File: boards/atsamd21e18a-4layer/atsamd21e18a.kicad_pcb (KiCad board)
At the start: 4 copper layers, 17.8 x 38.1 mm, 25 parts, among them J1 USB_B_Micro, J2 A, J3 B, J4 SWD_1.27, SW1 RESET, U1 AP7361C_SOT-89-5, U2 ATSAMD21E, Y1 <32MHz

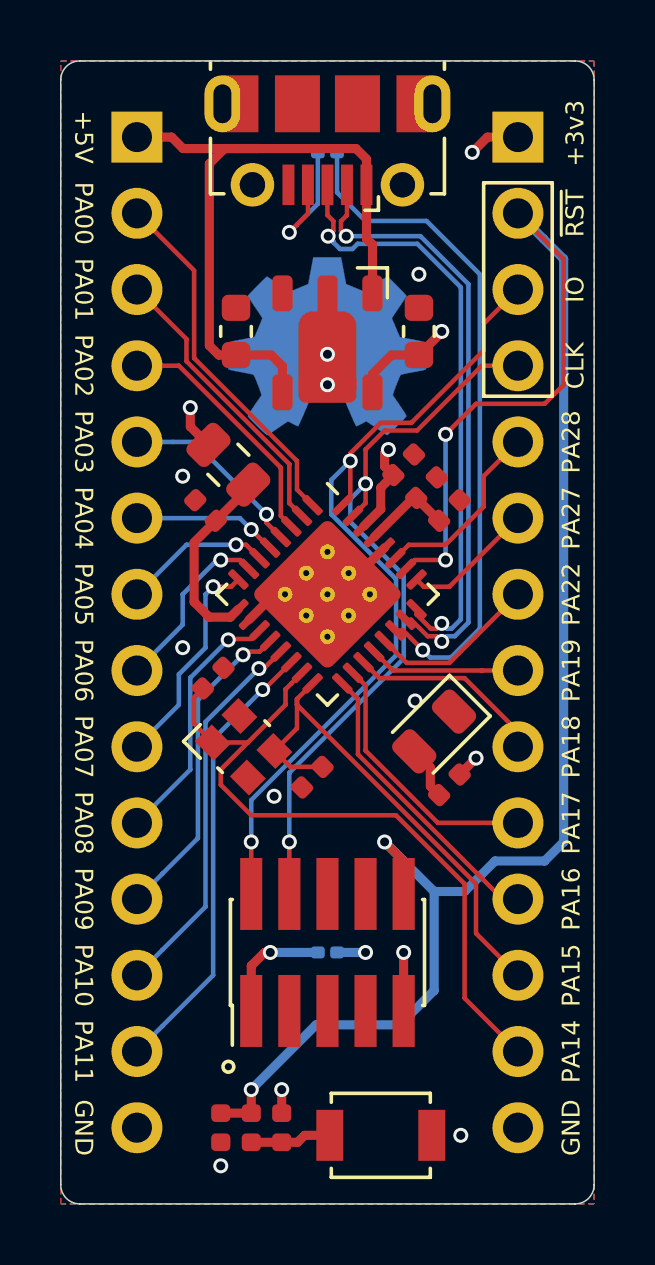
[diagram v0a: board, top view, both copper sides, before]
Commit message: Replaced 3225 crystal with 3215 on atsamd21e18a
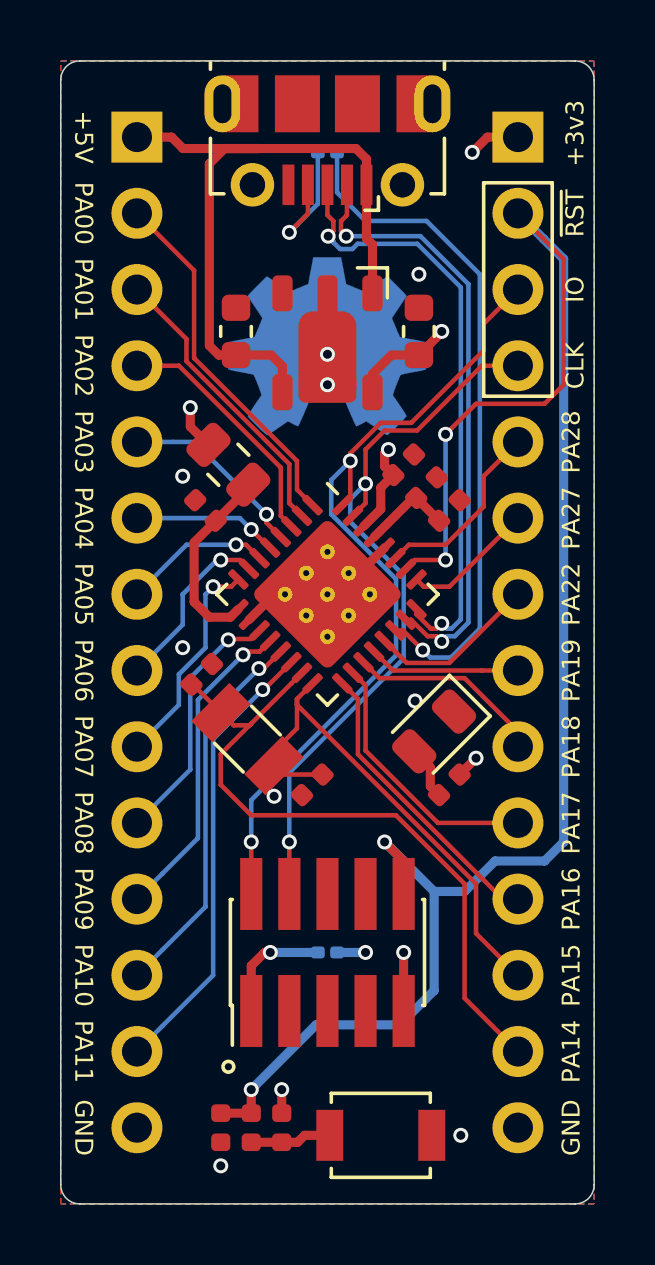
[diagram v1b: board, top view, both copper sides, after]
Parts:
- C7, C8: value 18n -> 22p
- Y1: value <32MHz -> ABS07-32.768KHZ; footprint Crystal:Crystal_SMD_Abracon_ABM10-4Pin_2.5x2.0mm -> Crystal:Crystal_SMD_3215-2Pin_3.2x1.5mm
- moved C7 0.40 mm to (31.4, 43.3)
- moved Y1 0.28 mm to (32.9, 45.5), turned to 135 degrees
- moved C8 0.25 mm to (35.1, 47.0)
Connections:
- Y1 pad 2: GND -> /PA15
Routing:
- net /PA14: track 24.0 -> 23.2 mm
- net /PA15: track 16.9 -> 16.8 mm, vias 0 -> 1
- net GND: vias 10 -> 9
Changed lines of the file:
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@@
     (thickness 1.6)
     (drawings 60)
-    (tracks 323)
+    (tracks 322)
     (zones 0)
     (modules 25)
@@
   )
   (setup
-    (last_trace_width 0.1016)
+    (last_trace_width 0.1524)
     (user_trace_width 0.1524)
     (user_trace_width 0.3048)
@@
     (add_net "Net-(U1-Pad3)")
   )
+  (module Crystal:Crystal_SMD_3215-2Pin_3.2x1.5mm (layer F.Cu)
+    (at 32.893 45.466 135)
+    (descr "SMD Crystal FC-135 https://support.epson.biz/td/api/doc_check.php?dl=brief_FC-135R_en.pdf")
+    (tags "SMD SMT Crystal")
+    (attr smd)
+    (fp_text reference Y1 (at 0 0 135) (layer F.SilkS) hide
+      (effects (font (size 1 1) (thickness 0.15)))
+    )
+    (fp_text value ABS07-32.768KHZ (at 0 2 135) (layer F.Fab)
+      (effects (font (size 1 1) (thickness 0.15)))
+    )
+    (fp_line (start 2 -1.15) (end 2 1.15) (layer F.CrtYd) (width 0.05))
+    (fp_line (start -2 -1.15) (end -2 1.15) (layer F.CrtYd) (width 0.05))
+    (fp_line (start -2 1.15) (end 2 1.15) (layer F.CrtYd) (width 0.05))
+    (fp_line (start -1.6 0.75) (end 1.6 0.75) (layer F.Fab) (width 0.1))
+    (fp_line (start -1.6 -0.75) (end 1.6 -0.75) (layer F.Fab) (width 0.1))
+    (fp_line (start 1.6 -0.75) (end 1.6 0.75) (layer F.Fab) (width 0.1))
+    (fp_line (start -0.675 -0.875) (end 0.675 -0.875) (layer F.SilkS) (width 0.12))
+    (fp_line (start -0.675 0.875) (end 0.675 0.875) (layer F.SilkS) (width 0.12))
+    (fp_line (start -1.6 -0.75) (end -1.6 0.75) (layer F.Fab) (width 0.1))
+    (fp_line (start -2 -1.15) (end 2 -1.15) (layer F.CrtYd) (width 0.05))
+    (fp_text user %R (at 0 -2 135) (layer F.Fab)
+      (effects (font (size 1 1) (thickness 0.15)))
+    )
+    (pad 2 smd rect (at -1.25 0 135) (size 1 1.8) (layers F.Cu F.Paste F.Mask)
+      (net 6 /PA15))
+    (pad 1 smd rect (at 1.25 0 135) (size 1 1.8) (layers F.Cu F.Paste F.Mask)
+      (net 5 /PA14))
+    (model ${KISYS3DMOD}/Crystal.3dshapes/Crystal_SMD_3215-2Pin_3.2x1.5mm.wrl
+      (at (xyz 0 0 0))
+      (scale (xyz 1 1 1))
+      (rotate (xyz 0 0 0))
+    )
+  )
   (module Symbol:OSHW-Symbol_6.7x6mm_Copper (layer B.Cu)
     (at 35.56 32.385 180)
@@
   )
   (module Capacitor_SMD:C_0402_1005Metric (layer F.Cu)
-    (at 35.052 46.736 225)
+    (at 35.052 46.99 225)
     (descr "Capacitor SMD 0402 (1005 Metric), square (rectangular) end terminal, IPC_7351 nominal, (Body size source: http://www.tortai-tech.com/upload/download/2011102023233369053.pdf), generated with kicad-footprint-generator")
     (tags capacitor)
@@
       (effects (font (size 1 1) (thickness 0.15)))
     )
-    (fp_text value 18n (at 0 1.17 45) (layer F.Fab)
+    (fp_text value 22p (at 0 1.17 45) (layer F.Fab)
       (effects (font (size 1 1) (thickness 0.15)))
     )
@@
   )
   (module Capacitor_SMD:C_0402_1005Metric (layer F.Cu)
-    (at 31.75 43.434 45)
+    (at 31.369 43.307 45)
     (descr "Capacitor SMD 0402 (1005 Metric), square (rectangular) end terminal, IPC_7351 nominal, (Body size source: http://www.tortai-tech.com/upload/download/2011102023233369053.pdf), generated with kicad-footprint-generator")
     (tags capacitor)
@@
       (effects (font (size 1 1) (thickness 0.15)))
     )
-    (fp_text value 18n (at 0 1.17 45) (layer F.Fab)
+    (fp_text value 22p (at 0 1.17 45) (layer F.Fab)
       (effects (font (size 1 1) (thickness 0.15)))
     )
@@
     (pad "" smd roundrect (at 0.345 0 180) (size 0.318 0.36) (layers B.Paste) (roundrect_rratio 0.25))
     (pad "" smd roundrect (at -0.345 0 180) (size 0.318 0.36) (layers B.Paste) (roundrect_rratio 0.25))
-  )
-  (module Crystal:Crystal_SMD_Abracon_ABM10-4Pin_2.5x2.0mm (layer F.Cu)
-    (at 32.766 45.72 45)
-    (descr "Abracon Miniature Ceramic Smd Crystal ABM10 http://www.abracon.com/Resonators/ABM10.pdf")
-    (tags "SMD SMT crystal Abracon ABM10")
-    (attr smd)
-    (fp_text reference Y1 (at 0 -2.5 45) (layer F.SilkS) hide
-      (effects (font (size 1 1) (thickness 0.15)))
-    )
-    (fp_text value <32MHz (at -0.179605 0 45) (layer F.Fab)
-      (effects (font (size 1 1) (thickness 0.15)))
-    )
-    (fp_line (start -1.53 -1.78) (end -1.53 1.78) (layer F.CrtYd) (width 0.05))
-    (fp_line (start -0.5 -1.54) (end -1.29 -1.54) (layer F.SilkS) (width 0.12))
-    (fp_line (start 1.11 -0.11) (end 1.11 0.11) (layer F.SilkS) (width 0.12))
-    (fp_line (start -1 -0.75) (end -1 1.25) (layer F.Fab) (width 0.1))
-    (fp_line (start 1 -1.25) (end 1 1.25) (layer F.Fab) (width 0.1))
-    (fp_line (start -0.5 -1.25) (end 1 -1.25) (layer F.Fab) (width 0.1))
-    (fp_line (start -1 1.25) (end 1 1.25) (layer F.Fab) (width 0.1))
-    (fp_line (start -1.11 -0.11) (end -1.11 0.11) (layer F.SilkS) (width 0.12))
-    (fp_line (start -0.5 -1.25) (end -1 -0.75) (layer F.Fab) (width 0.1))
-    (fp_line (start -1.29 -0.75) (end -1.29 -1.54) (layer F.SilkS) (width 0.12))
-    (fp_text user %R (at 0 0 135) (layer F.Fab)
-      (effects (font (size 0.5 0.5) (thickness 0.075)))
-    )
-    (fp_line (start 1.53 -1.78) (end 1.53 1.78) (layer F.CrtYd) (width 0.05))
-    (fp_line (start 1.53 -1.78) (end -1.53 -1.78) (layer F.CrtYd) (width 0.05))
-    (fp_line (start -1.53 1.78) (end 1.53 1.78) (layer F.CrtYd) (width 0.05))
-    (pad 4 smd rect (at 0.625 -0.825 45) (size 0.8 0.9) (layers F.Cu F.Paste F.Mask)
-      (net 2 GND))
-    (pad 2 smd rect (at -0.625 0.825 45) (size 0.8 0.9) (layers F.Cu F.Paste F.Mask)
-      (net 2 GND))
-    (pad 3 smd rect (at 0.625 0.825 45) (size 0.8 0.9) (layers F.Cu F.Paste F.Mask)
-      (net 6 /PA15))
-    (pad 1 smd rect (at -0.625 -0.825 45) (size 0.8 0.9) (layers F.Cu F.Paste F.Mask)
-      (net 5 /PA14))
-    (model ${KISYS3DMOD}/Crystal.3dshapes/Crystal_SMD_Abracon_ABM8G-4Pin_3.2x2.5mm.step
-      (at (xyz 0 0 0))
-      (scale (xyz 0.7812 0.8 0.8))
-      (rotate (xyz 0 0 90))
-    )
   )
   (module Package_DFN_QFN:QFN-32-1EP_5x5mm_P0.5mm_EP3.6x3.6mm_ThermalVias (layer F.Cu)
@@
   (via (at 35.56 33.655) (size 0.5) (drill 0.3) (layers F.Cu B.Cu) (net 2))
   (via (at 35.56 32.639) (size 0.5) (drill 0.3) (layers F.Cu B.Cu) (net 2))
-  (via (at 33.782 47.371) (size 0.5) (drill 0.3) (layers F.Cu B.Cu) (net 2))
+  (via (at 33.782 47.371) (size 0.5) (drill 0.3) (layers F.Cu B.Cu) (net 6))
   (via (at 38.099992 52.578) (size 0.5) (drill 0.3) (layers F.Cu B.Cu) (net 2))
   (segment (start 38.1 52.578008) (end 38.099992 52.578) (width 0.3048) (layer F.Cu) (net 2))
@@
   (segment (start 31.937 32.6645) (end 31.623 32.3505) (width 0.3048) (layer F.Cu) (net 4))
   (segment (start 34.35792 43.609847) (end 34.711472 43.256295) (width 0.1524) (layer F.Cu) (net 5))
-  (segment (start 34.163 43.804767) (end 34.35792 43.609847) (width 0.1524) (layer F.Cu) (net 5))
-  (segment (start 34.163 44.323) (end 34.163 43.804767) (width 0.1524) (layer F.Cu) (net 5))
-  (segment (start 32.907421 45.578579) (end 34.163 44.323) (width 0.1524) (layer F.Cu) (net 5))
-  (segment (start 31.740695 45.578579) (end 32.907421 45.578579) (width 0.1524) (layer F.Cu) (net 5))
-  (segment (start 31.115 44.952884) (end 31.740695 45.578579) (width 0.1524) (layer F.Cu) (net 5))
-  (segment (start 31.407053 43.776947) (end 31.115 44.069) (width 0.1524) (layer F.Cu) (net 5))
-  (segment (start 31.115 44.069) (end 31.115 44.952884) (width 0.1524) (layer F.Cu) (net 5))
-  (segment (start 40.132 54.102) (end 40.132 50.292) (width 0.1524) (layer F.Cu) (net 5))
   (segment (start 41.91 55.88) (end 40.132 54.102) (width 0.1524) (layer F.Cu) (net 5))
   (segment (start 40.132 50.292) (end 37.846 48.006) (width 0.1524) (layer F.Cu) (net 5))
   (segment (start 37.846 48.006) (end 33.02 48.006) (width 0.1524) (layer F.Cu) (net 5))
-  (segment (start 32.004 46.482) (end 32.907421 45.578579) (width 0.1524) (layer F.Cu) (net 5))
+  (segment (start 40.132 54.102) (end 40.132 50.292) (width 0.1524) (layer F.Cu) (net 5))
   (segment (start 33.02 48.006) (end 32.004 46.99) (width 0.1524) (layer F.Cu) (net 5))
-  (segment (start 32.004 46.99) (end 32.004 46.482) (width 0.1524) (layer F.Cu) (net 5))
+  (segment (start 32.004 46.99) (end 32.004 45.963767) (width 0.1524) (layer F.Cu) (net 5))
+  (segment (start 32.961388 45.00638) (end 33.014884 44.952884) (width 0.1524) (layer F.Cu) (net 5))
+  (segment (start 32.43338 45.00638) (end 32.961388 45.00638) (width 0.1524) (layer F.Cu) (net 5))
+  (segment (start 32.009117 44.582117) (end 32.43338 45.00638) (width 0.1524) (layer F.Cu) (net 5))
+  (segment (start 32.004 45.963767) (end 33.014884 44.952884) (width 0.1524) (layer F.Cu) (net 5))
+  (segment (start 33.014884 44.952884) (end 34.35792 43.609847) (width 0.1524) (layer F.Cu) (net 5))
+  (segment (start 31.076947 43.649947) (end 32.009117 44.582117) (width 0.1524) (layer F.Cu) (net 5))
+  (segment (start 31.026053 43.649947) (end 31.076947 43.649947) (width 0.1524) (layer F.Cu) (net 5))
   (segment (start 34.544 45.108726) (end 33.791305 45.861421) (width 0.1524) (layer F.Cu) (net 6))
   (segment (start 35.065025 43.609848) (end 34.544 44.130873) (width 0.1524) (layer F.Cu) (net 6))
   (segment (start 34.544 44.130873) (end 34.544 45.108726) (width 0.1524) (layer F.Cu) (net 6))
-  (segment (start 34.322937 46.393053) (end 33.791305 45.861421) (width 0.1524) (layer F.Cu) (net 6))
-  (segment (start 35.394947 46.393053) (end 34.322937 46.393053) (width 0.1524) (layer F.Cu) (net 6))
   (segment (start 34.544 44.323) (end 34.544 44.130873) (width 0.1524) (layer F.Cu) (net 6))
   (segment (start 40.513 50.292) (end 34.544 44.323) (width 0.1524) (layer F.Cu) (net 6))
   (segment (start 41.91 53.34) (end 40.513 51.943) (width 0.1524) (layer F.Cu) (net 6))
   (segment (start 40.513 51.943) (end 40.513 50.292) (width 0.1524) (layer F.Cu) (net 6))
+  (segment (start 34.074053 46.647053) (end 33.776883 46.349883) (width 0.1524) (layer F.Cu) (net 6))
+  (segment (start 35.394947 46.647053) (end 34.074053 46.647053) (width 0.1524) (layer F.Cu) (net 6))
   (segment (start 33.02 57.935) (end 32.004 57.935) (width 0.3048) (layer F.Cu) (net 7))
   (via (at 39.497 39.497) (size 0.5) (drill 0.3) (layers F.Cu B.Cu) (net 7))
